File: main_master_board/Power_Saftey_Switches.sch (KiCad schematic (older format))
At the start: 27 parts, among them P10 watchdog, P11 CONN_01X05, P12 motors_en, P9 uC_KS, Q1 PSMN013-80YS, Q2 LT1910, SW1 SWITCH_SPST, U13 74HC1G126, U14 PIC12(L)F1571/2

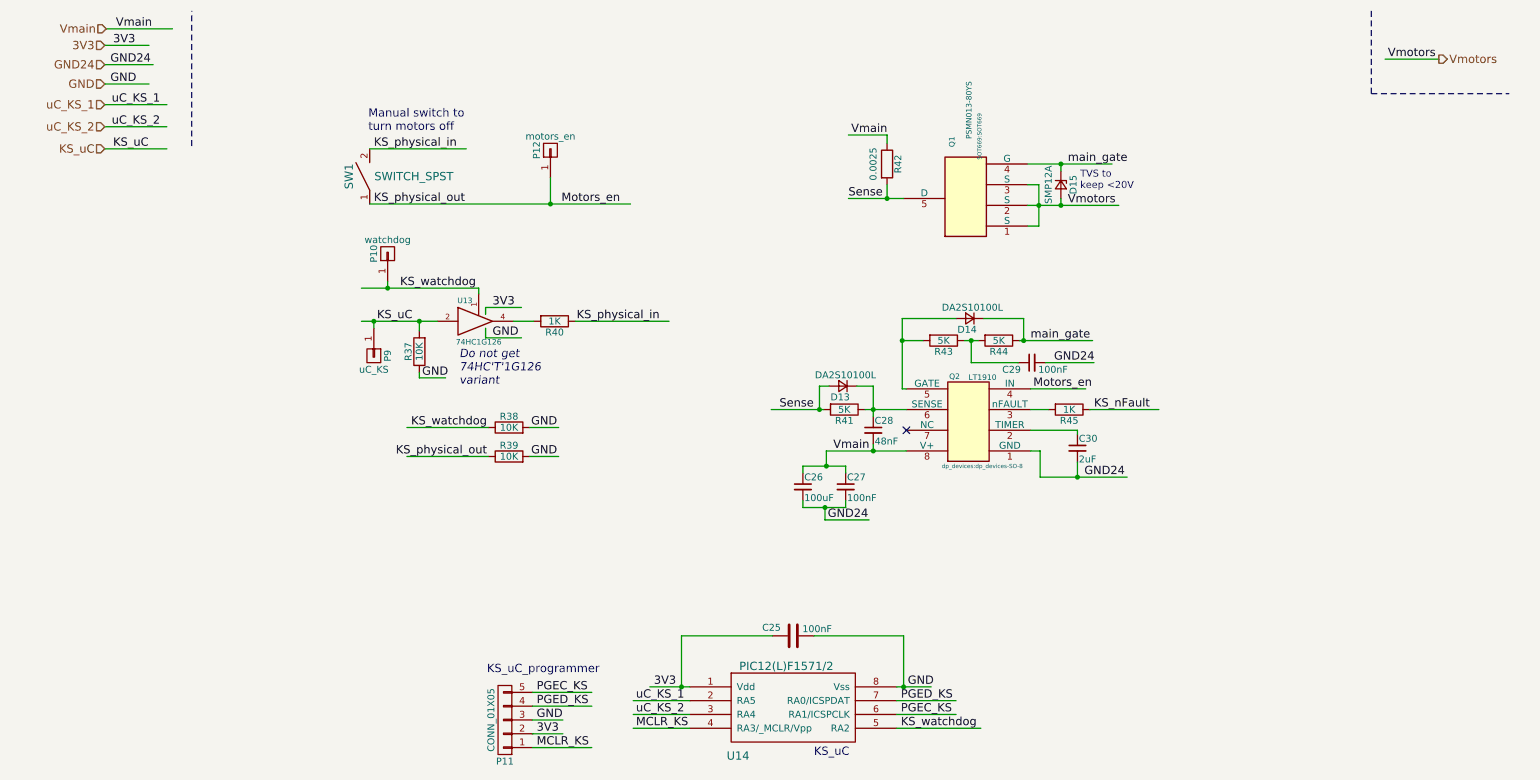
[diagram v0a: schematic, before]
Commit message: Started hooking up the dsPIC uC
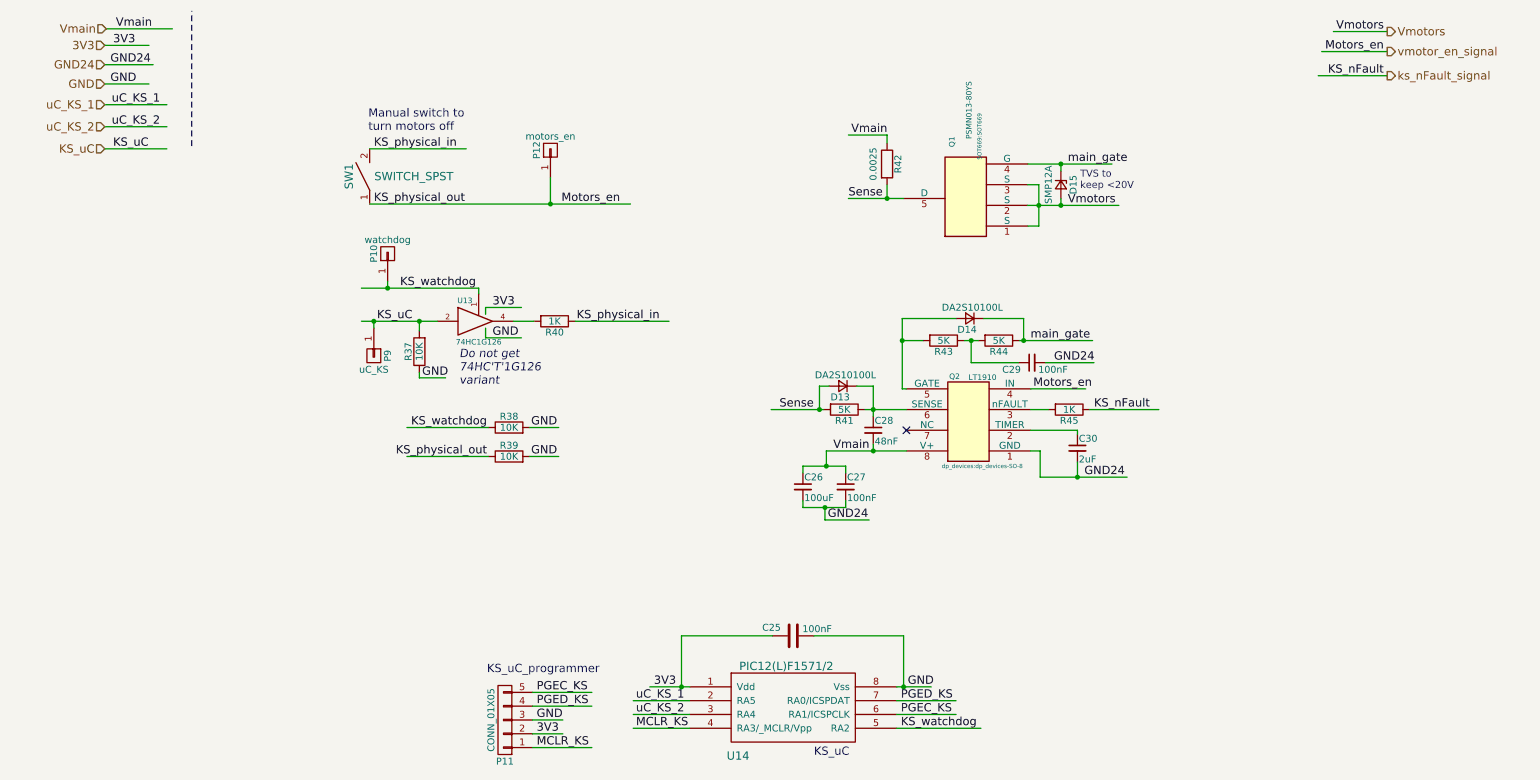
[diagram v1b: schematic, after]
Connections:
- net labels added: ks_nFault_signal, vmotor_en_signal
- wire segments 94 -> 117
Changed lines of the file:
@@
 LIBS:EDISON-SchDoc-cache
 LIBS:ETHERNET_USB_HUB-SchDoc-cache
-LIBS:PIC-SchDoc-cache
 LIBS:RF-SchDoc-cache
-LIBS:topsheet_Controller-SchDoc-cache
 LIBS:topsheet_Master-SchDoc-cache
-LIBS:topsheet_Power-SchDoc-cache
 LIBS:USB_CONSOL-SchDoc-cache
 LIBS:VBAT_PROTECTION_REGS-SchDoc-cache
+LIBS:PIC-SchDoc-cache
+LIBS:topsheet_Controller-SchDoc-cache
+LIBS:topsheet_Power-SchDoc-cache
 LIBS:TPS754
 LIBS:FDS4935A
@@
 LIBS:TPS832130SIL
 LIBS:SS4-50-3.00-X-D
+LIBS:74xgxx
+LIBS:ac-dc
+LIBS:actel
+LIBS:allegro
+LIBS:Altera
+LIBS:analog_devices
+LIBS:battery_management
+LIBS:bbd
+LIBS:brooktre
+LIBS:cmos_ieee
+LIBS:dc-dc
+LIBS:diode
+LIBS:elec-unifil
+LIBS:ESD_Protection
+LIBS:ftdi
+LIBS:gennum
+LIBS:graphic
+LIBS:hc11
+LIBS:ir
+LIBS:Lattice
+LIBS:logo
+LIBS:maxim
+LIBS:mechanical
+LIBS:microchip_dspic33dsc
+LIBS:microchip_pic10mcu
+LIBS:microchip_pic12mcu
+LIBS:microchip_pic16mcu
+LIBS:microchip_pic18mcu
+LIBS:microchip_pic32mcu
+LIBS:motor_drivers
+LIBS:motors
+LIBS:msp430
+LIBS:nordicsemi
+LIBS:nxp_armmcu
+LIBS:onsemi
+LIBS:Oscillators
+LIBS:Power_Management
+LIBS:powerint
+LIBS:pspice
+LIBS:references
+LIBS:relays
+LIBS:rfcom
+LIBS:sensors
+LIBS:silabs
+LIBS:stm8
+LIBS:stm32
+LIBS:supertex
+LIBS:switches
+LIBS:transf
+LIBS:ttl_ieee
+LIBS:video
+LIBS:wiznet
+LIBS:Worldsemi
+LIBS:Xicor
+LIBS:zetex
+LIBS:Zilog
 LIBS:main_master_board-cache
 EELAYER 25 0
@@
 uC_KS_2
 Wire Wire Line
-	7720 1590 8330 1590
+	7720 1590 7960 1590
+Wire Wire Line
+	7960 1590 8330 1590
 Wire Wire Line
 	7720 1740 7800 1740
 Wire Wire Line
-	7800 1740 7800 2040
+	7800 1740 7800 1890
+Wire Wire Line
+	7800 1890 7800 2040
 Wire Wire Line
 	7800 2040 7720 2040
 Wire Wire Line
-	7720 1890 8380 1890
+	7720 1890 7800 1890
+Wire Wire Line
+	7800 1890 7960 1890
+Wire Wire Line
+	7960 1890 8380 1890
 Connection ~ 7800 1890
 Wire Wire Line
@@
 	6700 1740 6700 1840
 Wire Wire Line
-	6420 1840 6820 1840
+	6420 1840 6700 1840
+Wire Wire Line
+	6700 1840 6820 1840
 Wire Wire Line
 	6700 1440 6700 1380
@@
 Connection ~ 6700 1840
 Wire Wire Line
-	6540 3370 6840 3370
-Wire Wire Line
-	6600 3200 6600 3420
+	6540 3370 6600 3370
+Wire Wire Line
+	6600 3370 6840 3370
+Wire Wire Line
+	6600 3200 6600 3370
+Wire Wire Line
+	6600 3370 6600 3420
 Connection ~ 6600 3370
 Wire Wire Line
 	6600 3620 6600 3670
 Wire Wire Line
-	6260 3670 6840 3670
+	6260 3670 6600 3670
+Wire Wire Line
+	6600 3670 6840 3670
 Connection ~ 6600 3670
 Wire Wire Line
 	6480 3200 6600 3200
 Wire Wire Line
-	5860 3370 6240 3370
+	5860 3370 6210 3370
+Wire Wire Line
+	6210 3370 6240 3370
 Wire Wire Line
 	6280 3200 6210 3200
@@
 	7810 3670 7810 3860
 Wire Wire Line
-	7810 3860 8440 3860
+	7810 3860 8080 3860
+Wire Wire Line
+	8080 3860 8440 3860
 Wire Wire Line
 	8080 3750 8080 3860
@@
 	6810 3220 6840 3220
 Wire Wire Line
-	6810 2710 6810 3220
+	6810 2710 6810 2870
+Wire Wire Line
+	6810 2870 6810 3220
 Wire Wire Line
 	6810 2870 6960 2870
 Wire Wire Line
-	7260 2870 7360 2870
-Wire Wire Line
-	7660 2870 8190 2870
+	7260 2870 7310 2870
+Wire Wire Line
+	7310 2870 7360 2870
+Wire Wire Line
+	7660 2870 7690 2870
+Wire Wire Line
+	7690 2870 8190 2870
 Wire Wire Line
 	7400 2710 7690 2710
@@
 	6090 3830 6090 3780
 Wire Wire Line
-	6090 3780 6400 3780
+	6090 3780 6260 3780
+Wire Wire Line
+	6260 3780 6400 3780
 Wire Wire Line
 	6400 3780 6400 3830
@@
 	6090 4030 6090 4080
 Wire Wire Line
-	6090 4080 6400 4080
+	6090 4080 6250 4080
+Wire Wire Line
+	6250 4080 6400 4080
 Wire Wire Line
 	6400 4080 6400 4030
@@
 	3790 2630 4050 2630
 Wire Wire Line
-	2890 2730 3440 2730
+	2890 2730 2980 2730
+Wire Wire Line
+	2980 2730 3310 2730
+Wire Wire Line
+	3310 2730 3440 2730
 Wire Wire Line
 	3310 2730 3310 2800
@@
 	3740 2490 3740 2530
 Wire Wire Line
-	2890 2490 3740 2490
+	2890 2490 3080 2490
+Wire Wire Line
+	3080 2490 3740 2490
 Connection ~ 3310 2730
 Wire Wire Line
@@
 	6820 5010 6820 5380
 Wire Wire Line
-	6770 5380 7020 5380
-Wire Wire Line
-	4980 5380 5270 5380
+	6770 5380 6820 5380
+Wire Wire Line
+	6820 5380 7020 5380
+Wire Wire Line
+	4980 5380 5210 5380
+Wire Wire Line
+	5210 5380 5270 5380
 Wire Wire Line
 	5210 5380 5210 5010
@@
 Wire Notes Line
 	1660 1460 1660 480
-Text HLabel 10700 830  2    60   Output ~ 0
+Text HLabel 10325 630  2    60   Output ~ 0
 Vmotors
 Wire Wire Line
-	10700 830  10310 830
-Text Label 10330 830  0    60   ~ 0
+	10325 630  9935 630
+Text Label 9955 630  0    60   ~ 0
 Vmotors
 $Comp
@@
 $EndComp
 Wire Wire Line
-	2950 1880 4840 1880
+	2950 1880 4260 1880
+Wire Wire Line
+	4260 1880 4840 1880
 Wire Wire Line
 	2950 1480 3650 1480
@@
 Text Label 1090 1480 0    60   ~ 0
 KS_uC
-Wire Notes Line
-	10210 480  10210 1080
-Wire Notes Line
-	10210 1080 11210 1080
 Text HLabel 1030 1010 0    60   Input ~ 0
 GND
@@
 Text Label 1070 1010 0    60   ~ 0
 GND
+Text HLabel 10325 775  2    60   Output ~ 0
+vmotor_en_signal
+Wire Wire Line
+	10325 775  9850 775
+Text Label 10300 775  2    60   ~ 0
+Motors_en
+Text HLabel 10325 950  2    60   Output ~ 0
+ks_nFault_signal
+Wire Wire Line
+	10325 950  9825 950
+Text Label 10300 950  2    60   ~ 0
+KS_nFault
 $EndSCHEMATC

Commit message: Started adding support for a new snapdragon board. Dart0410
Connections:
- wire segments 117 -> 96
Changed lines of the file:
@@
 LIBS:FDS4935A
 LIBS:Si1900DL
-LIBS:Amplifiers
-LIBS:Connectors
-LIBS:DataStorage
-LIBS:Diodes
-LIBS:Microprocessors
-LIBS:MiscellaneousDevices
-LIBS:Passives
-LIBS:PMOD
-LIBS:PowerComponents
-LIBS:RepeaterParts
-LIBS:RF_OEM_Parts
 LIBS:Sensors
-LIBS:TransistorParts
 LIBS:LP3852-3.3
 LIBS:0s102011ma1qn1
@@
 LIBS:xal5050-562meb
 LIBS:xal6030-182mec
-LIBS:decaWave
 LIBS:conn_2x50
 LIBS:conn_open_q_x2
@@
 LIBS:ac-dc
 LIBS:actel
-LIBS:allegro
 LIBS:Altera
 LIBS:analog_devices
@@
 LIBS:logo
 LIBS:maxim
-LIBS:mechanical
 LIBS:microchip_dspic33dsc
 LIBS:microchip_pic10mcu
@@
 LIBS:microchip_pic32mcu
 LIBS:motor_drivers
-LIBS:motors
 LIBS:msp430
 LIBS:nordicsemi
@@
 LIBS:ttl_ieee
 LIBS:video
-LIBS:wiznet
 LIBS:Worldsemi
 LIBS:Xicor
-LIBS:zetex
 LIBS:Zilog
 LIBS:main_master_board-cache
@@
 uC_KS_2
 Wire Wire Line
-	7720 1590 7960 1590
-Wire Wire Line
-	7960 1590 8330 1590
+	7720 1590 8330 1590
 Wire Wire Line
 	7720 1740 7800 1740
 Wire Wire Line
-	7800 1740 7800 1890
-Wire Wire Line
-	7800 1890 7800 2040
+	7800 1740 7800 2040
 Wire Wire Line
 	7800 2040 7720 2040
 Wire Wire Line
-	7720 1890 7800 1890
-Wire Wire Line
-	7800 1890 7960 1890
-Wire Wire Line
-	7960 1890 8380 1890
+	7720 1890 8380 1890
 Connection ~ 7800 1890
 Wire Wire Line
@@
 	6700 1740 6700 1840
 Wire Wire Line
-	6420 1840 6700 1840
-Wire Wire Line
-	6700 1840 6820 1840
+	6420 1840 6820 1840
 Wire Wire Line
 	6700 1440 6700 1380
@@
 Connection ~ 6700 1840
 Wire Wire Line
-	6540 3370 6600 3370
-Wire Wire Line
-	6600 3370 6840 3370
-Wire Wire Line
-	6600 3200 6600 3370
-Wire Wire Line
-	6600 3370 6600 3420
+	6540 3370 6840 3370
+Wire Wire Line
+	6600 3200 6600 3420
 Connection ~ 6600 3370
 Wire Wire Line
 	6600 3620 6600 3670
 Wire Wire Line
-	6260 3670 6600 3670
-Wire Wire Line
-	6600 3670 6840 3670
+	6260 3670 6840 3670
 Connection ~ 6600 3670
 Wire Wire Line
 	6480 3200 6600 3200
 Wire Wire Line
-	5860 3370 6210 3370
-Wire Wire Line
-	6210 3370 6240 3370
+	5860 3370 6240 3370
 Wire Wire Line
 	6280 3200 6210 3200
@@
 	7810 3670 7810 3860
 Wire Wire Line
-	7810 3860 8080 3860
-Wire Wire Line
-	8080 3860 8440 3860
+	7810 3860 8440 3860
 Wire Wire Line
 	8080 3750 8080 3860
@@
 	6810 3220 6840 3220
 Wire Wire Line
-	6810 2710 6810 2870
-Wire Wire Line
-	6810 2870 6810 3220
+	6810 2710 6810 3220
 Wire Wire Line
 	6810 2870 6960 2870
 Wire Wire Line
-	7260 2870 7310 2870
-Wire Wire Line
-	7310 2870 7360 2870
-Wire Wire Line
-	7660 2870 7690 2870
-Wire Wire Line
-	7690 2870 8190 2870
+	7260 2870 7360 2870
+Wire Wire Line
+	7660 2870 8190 2870
 Wire Wire Line
 	7400 2710 7690 2710
@@
 	6090 3830 6090 3780
 Wire Wire Line
-	6090 3780 6260 3780
-Wire Wire Line
-	6260 3780 6400 3780
+	6090 3780 6400 3780
 Wire Wire Line
 	6400 3780 6400 3830
@@
 	6090 4030 6090 4080
 Wire Wire Line
-	6090 4080 6250 4080
-Wire Wire Line
-	6250 4080 6400 4080
+	6090 4080 6400 4080
 Wire Wire Line
 	6400 4080 6400 4030
@@
 	3790 2630 4050 2630
 Wire Wire Line
-	2890 2730 2980 2730
-Wire Wire Line
-	2980 2730 3310 2730
-Wire Wire Line
-	3310 2730 3440 2730
+	2890 2730 3440 2730
 Wire Wire Line
 	3310 2730 3310 2800
@@
 	3740 2490 3740 2530
 Wire Wire Line
-	2890 2490 3080 2490
-Wire Wire Line
-	3080 2490 3740 2490
+	2890 2490 3740 2490
 Connection ~ 3310 2730
 Wire Wire Line
@@
 	6820 5010 6820 5380
 Wire Wire Line
-	6770 5380 6820 5380
-Wire Wire Line
-	6820 5380 7020 5380
-Wire Wire Line
-	4980 5380 5210 5380
-Wire Wire Line
-	5210 5380 5270 5380
+	6770 5380 7020 5380
+Wire Wire Line
+	4980 5380 5270 5380
 Wire Wire Line
 	5210 5380 5210 5010
@@
 $EndComp
 Wire Wire Line
-	2950 1880 4260 1880
-Wire Wire Line
-	4260 1880 4840 1880
+	2950 1880 4840 1880
 Wire Wire Line
 	2950 1480 3650 1480

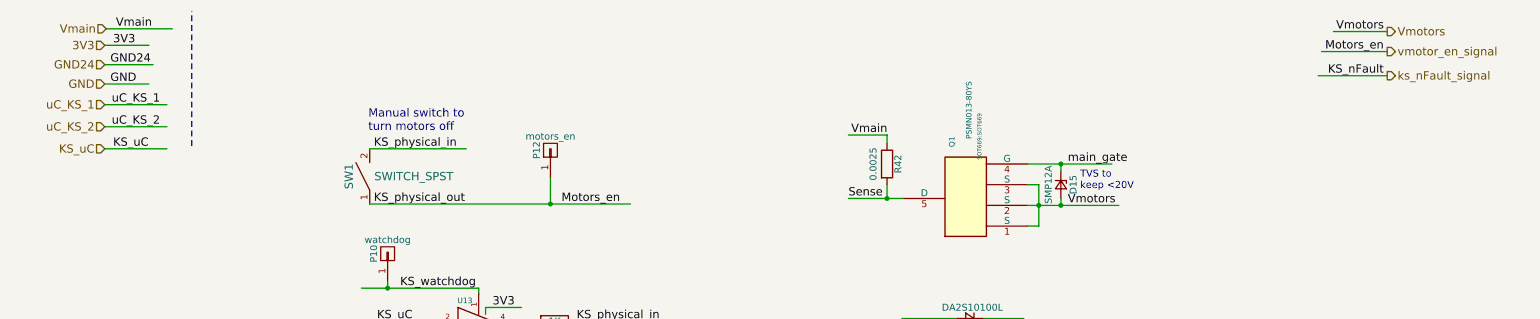
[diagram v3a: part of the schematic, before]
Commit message: Working on moving things to two boards
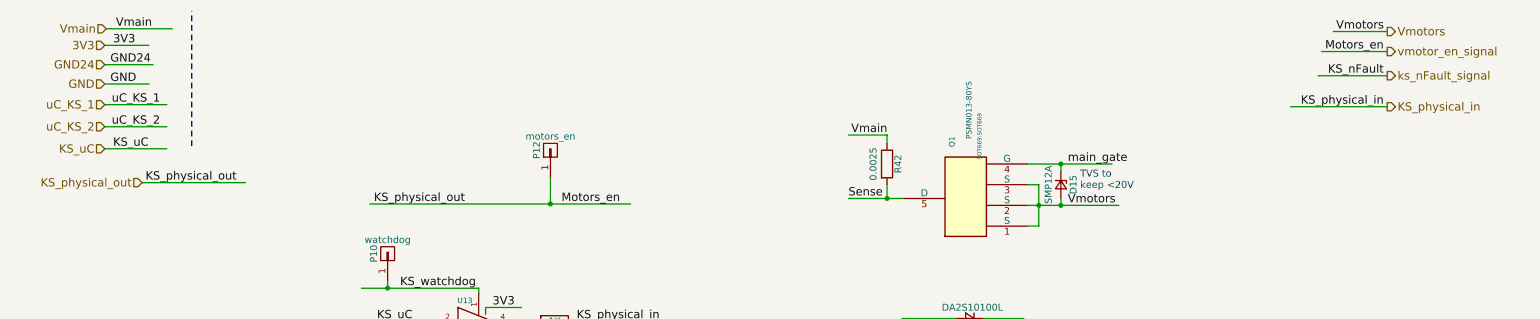
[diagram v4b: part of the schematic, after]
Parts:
- removed SW1: SWITCH_SPST, molex_microclasp2:microclasp_vdrx2, symbol SWITCH_SPST
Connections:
- wire segments 96 -> 97
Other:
- note removed: "Manual switch to \nturn motors off"
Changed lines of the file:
@@
 LIBS:FDS4935A
 LIBS:Si1900DL
-LIBS:Amplifiers
-LIBS:Connectors
-LIBS:DataStorage
-LIBS:Diodes
-LIBS:Microprocessors
-LIBS:MiscellaneousDevices
-LIBS:Passives
-LIBS:PMOD
-LIBS:PowerComponents
-LIBS:RepeaterParts
-LIBS:RF_OEM_Parts
 LIBS:Sensors
-LIBS:TransistorParts
 LIBS:LP3852-3.3
 LIBS:0s102011ma1qn1
@@
 LIBS:xal5050-562meb
 LIBS:xal6030-182mec
-LIBS:decaWave
 LIBS:conn_2x50
 LIBS:conn_open_q_x2
@@
 LIBS:ac-dc
 LIBS:actel
-LIBS:allegro
 LIBS:Altera
 LIBS:analog_devices
@@
 LIBS:logo
 LIBS:maxim
-LIBS:mechanical
 LIBS:microchip_dspic33dsc
 LIBS:microchip_pic10mcu
@@
 LIBS:microchip_pic32mcu
 LIBS:motor_drivers
-LIBS:motors
 LIBS:msp430
 LIBS:nordicsemi
@@
 LIBS:ttl_ieee
 LIBS:video
-LIBS:wiznet
 LIBS:Worldsemi
 LIBS:Xicor
-LIBS:zetex
 LIBS:Zilog
 LIBS:conn_2x45
@@
 Text Label 9955 630  0    60   ~ 0
 Vmotors
-$Comp
-L SWITCH_SPST SW1
-U 1 1 58711BE2
-P 2950 1680
-F 0 "SW1" H 2950 1830 60  0000 C CNN
-F 1 "SWITCH_SPST" V 2950 1360 60  0000 C CNN
-F 2 "molex_microclasp2:microclasp_vdrx2" H 2950 1680 60  0001 C CNN
-F 3 "" H 2950 1680 60  0000 C CNN
-	1    2950 1680
-	0    -1   -1   0
-$EndComp
 Wire Wire Line
 	2950 1880 4840 1880
-Wire Wire Line
-	2950 1480 3650 1480
 Text Label 2980 1880 0    60   ~ 0
 KS_physical_out
-Text Label 2980 1480 0    60   ~ 0
-KS_physical_in
-Text Notes 2940 1360 0    60   ~ 0
-Manual switch to \nturn motors off
 $Comp
 L CONN_01X01 P12
@@
 Text Label 10300 950  2    60   ~ 0
 KS_nFault
+Text HLabel 10325 1175 2    60   Output ~ 0
+KS_physical_in
+Text HLabel 1300 1725 0    60   Input ~ 0
+KS_physical_out
+Wire Wire Line
+	1300 1725 2050 1725
+Text Label 1325 1725 0    60   ~ 0
+KS_physical_out
+Wire Wire Line
+	9625 1175 10325 1175
+Text Label 10300 1175 2    60   ~ 0
+KS_physical_in
 $EndSCHEMATC
